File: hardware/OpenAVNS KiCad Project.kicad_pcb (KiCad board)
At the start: 4 copper layers, 69.9 x 100.9 mm, 216 parts, among them J1 Conn_ARM_JTAG_SWD_10, J2 AudioPlug3, J3 USB_C_Receptacle, J4 Conn_01x02_Pin, J5 Conn_01x03_Pin, J6 Conn_01x01_Pin, Q1 BCV62, Q2 BC847, Q3 BC857, Q4 BCV61, Q5 BCV62, Q6 BC847, Q7 BC857, Q8 BCV61, SW1 SW_SPDT, T1 Wurth 750315839 - 1:10, 40uH, U1 TS5A3159AYZPR, U10 TLV9062, U11 LIS2DH12, U12 OPA455, U13 74AUC1G74, U14 TPS61200DRC, U15 LT1615ES5_TRPBF, U16 LT8304IS8E_PBF, U17 MCP73831-2-OT, U2 TLV9004xRUCR, U3 MCP4725xxx-xCH, U4 TS5A3159AYZPR, U5 nRF52840, U6 TS5A3159AYZPR, U7 MCP4725xxx-xCH, U8 TS5A3159AYZPR, U9 OPA455, Y1 32MHz - X322532MOB4SI

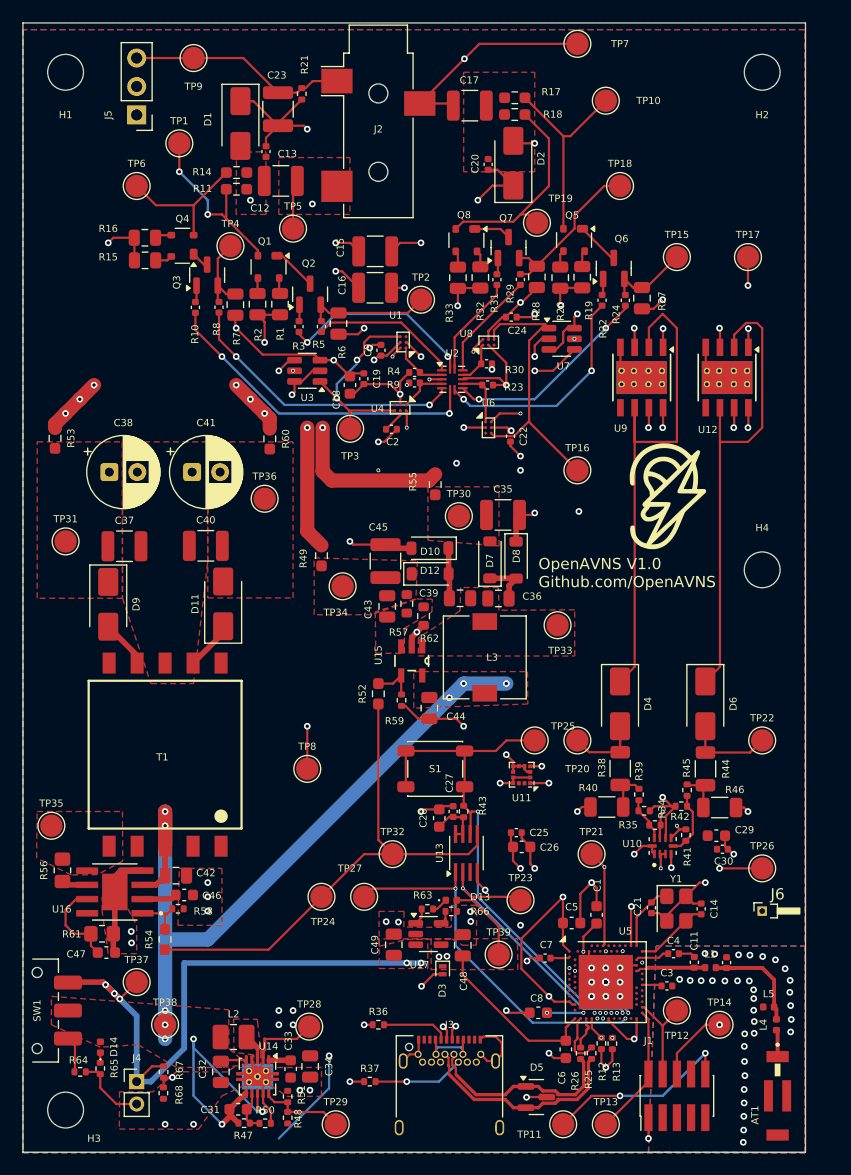
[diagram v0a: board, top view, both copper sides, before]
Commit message: Fixed hole clearance DRC errors
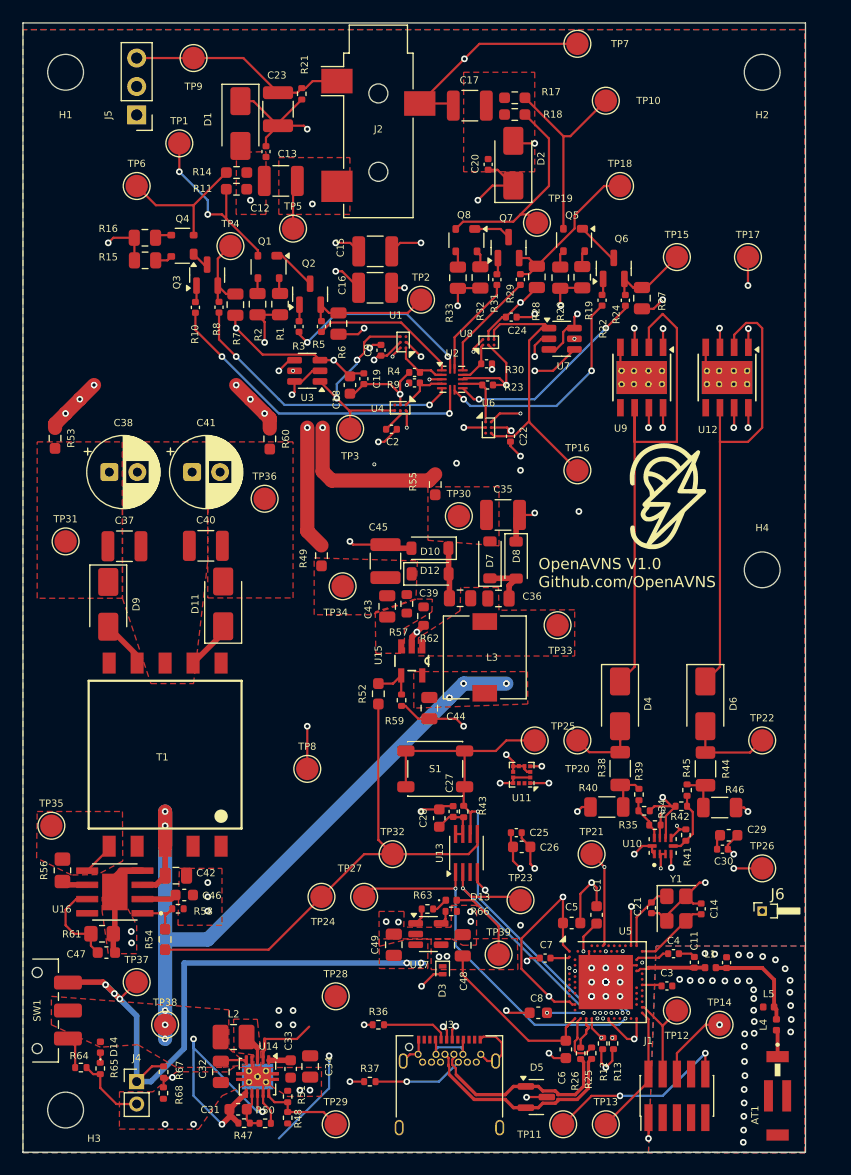
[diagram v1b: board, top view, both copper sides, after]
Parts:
- moved TP28 3.60 mm to (86.4, 132.1)
- moved C29 1.10 mm to (121.5, 117.7)
- moved R64 0.39 mm to (63.6, 138.4)
- moved R12 0.12 mm to (110.2, 136.3)
- moved R13 0.10 mm to (111.2, 136.3)
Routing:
- net Net-(U16-SW): track 0.00 -> 2.99 mm
- net +3.3V: track 155.3 -> 156.8 mm
- net /C2A_ON: track 78.8 -> 80.3 mm
- net /I2C_SDA: track 94.4 -> 95.4 mm

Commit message: Edited based on Maros advice, thanks
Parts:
- moved TP1 5.39 mm to (68.6, 59.7)
- moved TP6 5.39 mm to (72.4, 55.9)
- moved C32 1.93 mm to (74.2, 138.7)
- moved C31 1.53 mm to (76.3, 141.5), turned to -90 degrees
- moved L2 1.02 mm to (76.7, 134.9)
- moved R54 0.67 mm to (71.8, 127.0)
- moved R50 0.56 mm to (80.6, 143.4)
- moved R58 0.42 mm to (72.2, 124.7)
- moved C46 0.32 mm to (72.8, 123.3)
- moved L5 0.31 mm to (125.3, 133.1)
- moved R47 0.14 mm to (78.3, 143.4)
- moved L4 0.13 mm to (125.8, 134.7)
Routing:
- net GND: track 173.2 -> 161.4 mm
- net Net-(U7-VOUT): track 25.8 -> 32.8 mm
- net +3.3V: track 156.8 -> 150.7 mm, vias 26 -> 23
- net Net-(D6-K): track 42.4 -> 46.0 mm
- net Net-(U14-UVLO): track 3.85 -> 6.61 mm
- net Net-(D4-K): track 47.3 -> 44.5 mm
- net /C2_Anodic: track 18.2 -> 20.4 mm
- net /C1_Cathodic: track 12.6 -> 14.0 mm, vias 0 -> 2
- net /C1_Anodic: track 16.3 -> 15.2 mm, vias 2 -> 0
- net Net-(U14-L): track 2.46 -> 3.55 mm
- net /V_ON: track 95.9 -> 96.9 mm
- net /50V_ON: track 4.92 -> 4.07 mm
- net Net-(J1-SWCLK/TCK): track 8.71 -> 9.42 mm
- net /HV_ON: track 46.7 -> 46.0 mm
- net Net-(U3-VOUT): track 18.9 -> 19.5 mm
- removed copper zone on F.Cu, net Net-(U14-L)

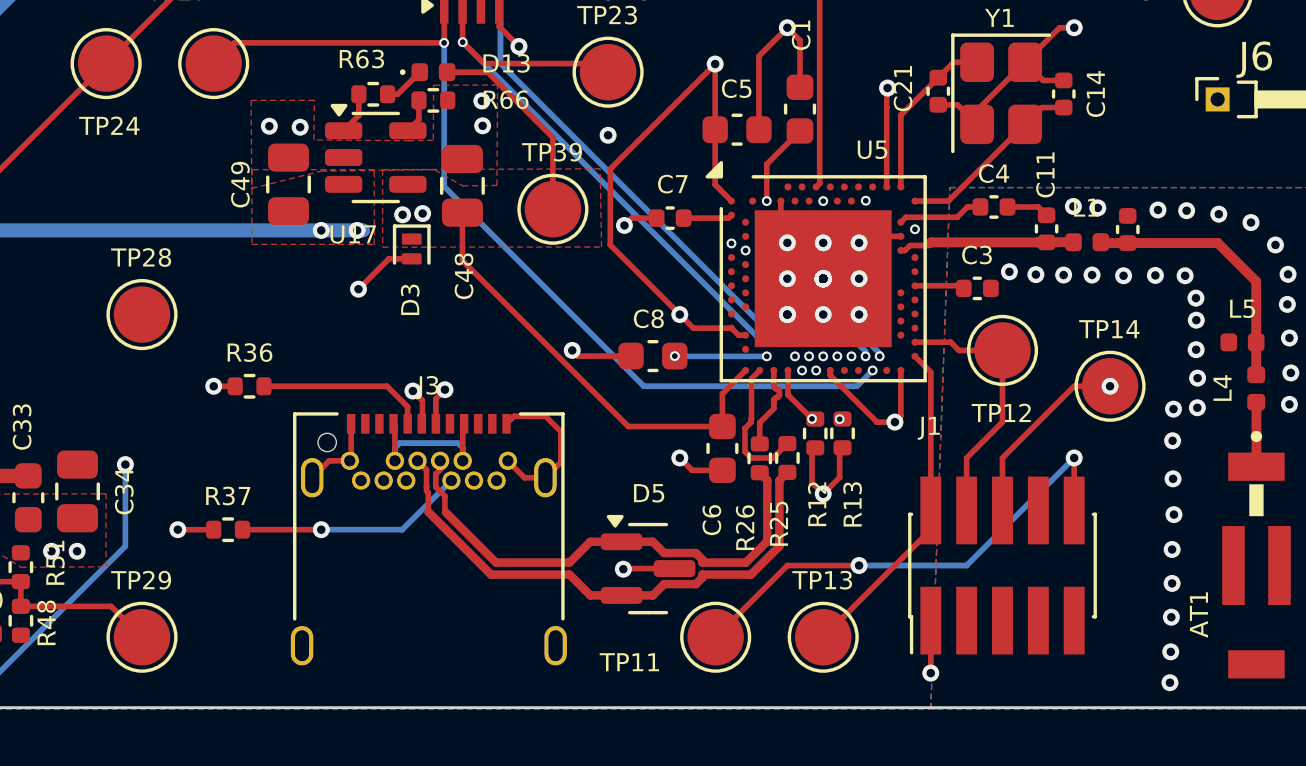
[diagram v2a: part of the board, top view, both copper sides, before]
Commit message: Updated USB connector and routing
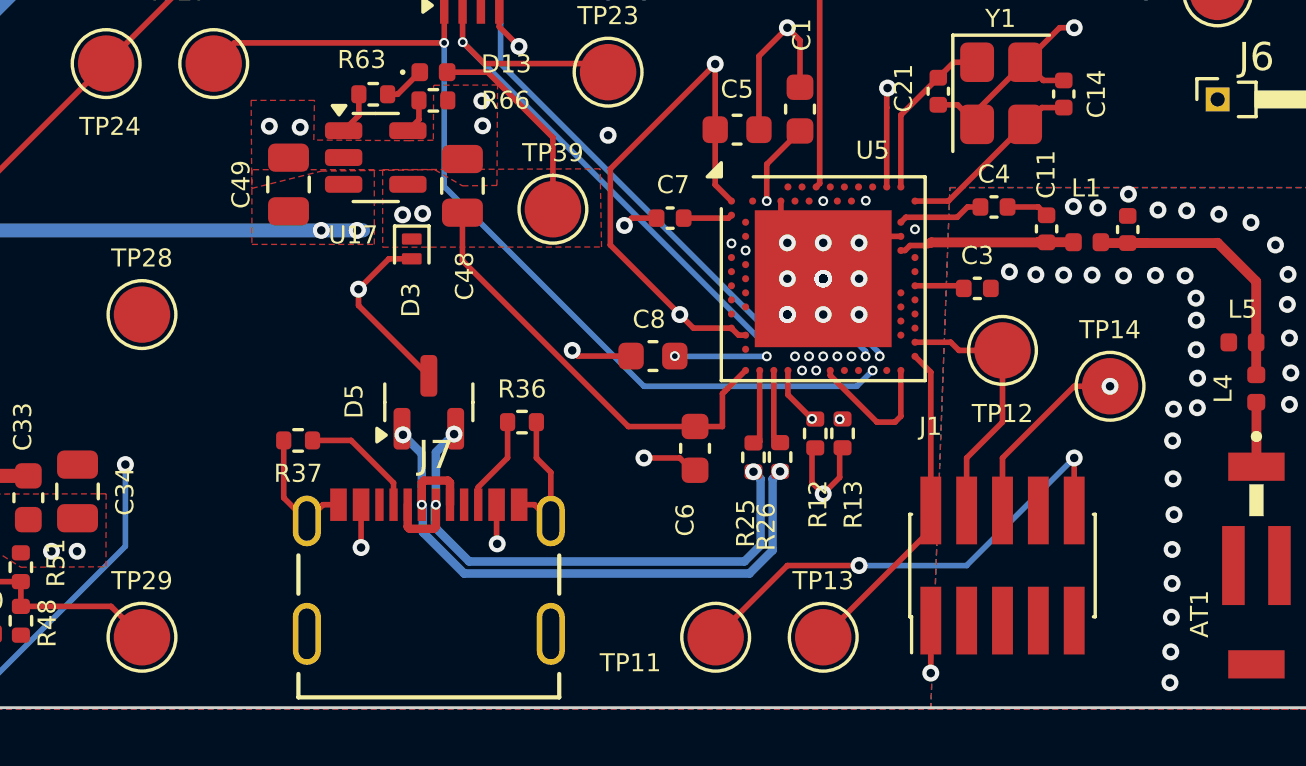
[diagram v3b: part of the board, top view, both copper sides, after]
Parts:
- removed J3: USB_C_Receptacle, Connector_USB:USB_C_Receptacle_Amphenol_12401548E4-2A
- added J7: 2171790001, Footprints:MOLEX_2171790001, F.Cu at (96.5, 142.2)
- R15: value R_US -> 1k
- R16: value R_US -> 150 Ohm
- R29: value R_US -> 100 Ohm
- moved D5 9.75 mm to (96.5, 135.2), turned to 90 degrees
- moved R36 9.73 mm to (99.8, 135.9)
- moved R37 4.02 mm to (91.9, 136.5), turned to 180 degrees
- moved R25 1.20 mm to (108.0, 137.1)
- moved C6 0.97 mm to (106.0, 136.8)
- moved R26 0.72 mm to (109.0, 137.1)
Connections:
- R36 pad 1: GND -> Net-(J7-CC2)
- R36 pad 2: Net-(J3-CC1) -> GND
- R37 pad 1: GND -> Net-(J7-CC1)
- R37 pad 2: Net-(J3-CC2) -> GND
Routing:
- net Net-(J3-CC2): track 8.12 -> 0.00 mm, vias 1 -> 0
- net Net-(J3-CC1): track 5.99 -> 0.00 mm
- net /V_USB: track 31.8 -> 25.8 mm, vias 2 -> 4
- net Net-(J7-CC1): track 0.00 -> 4.27 mm
- net Net-(J7-CC2): track 0.00 -> 3.36 mm
- net /MCU_D-: track 4.90 -> 2.64 mm
- net /USB_D-: track 23.4 -> 21.2 mm, vias 1 -> 3
- net GND: track 161.4 -> 163.3 mm, vias 111 -> 109
- net /USB_D+: track 22.0 -> 22.6 mm, vias 1 -> 3
- net +3.3V: vias 23 -> 22

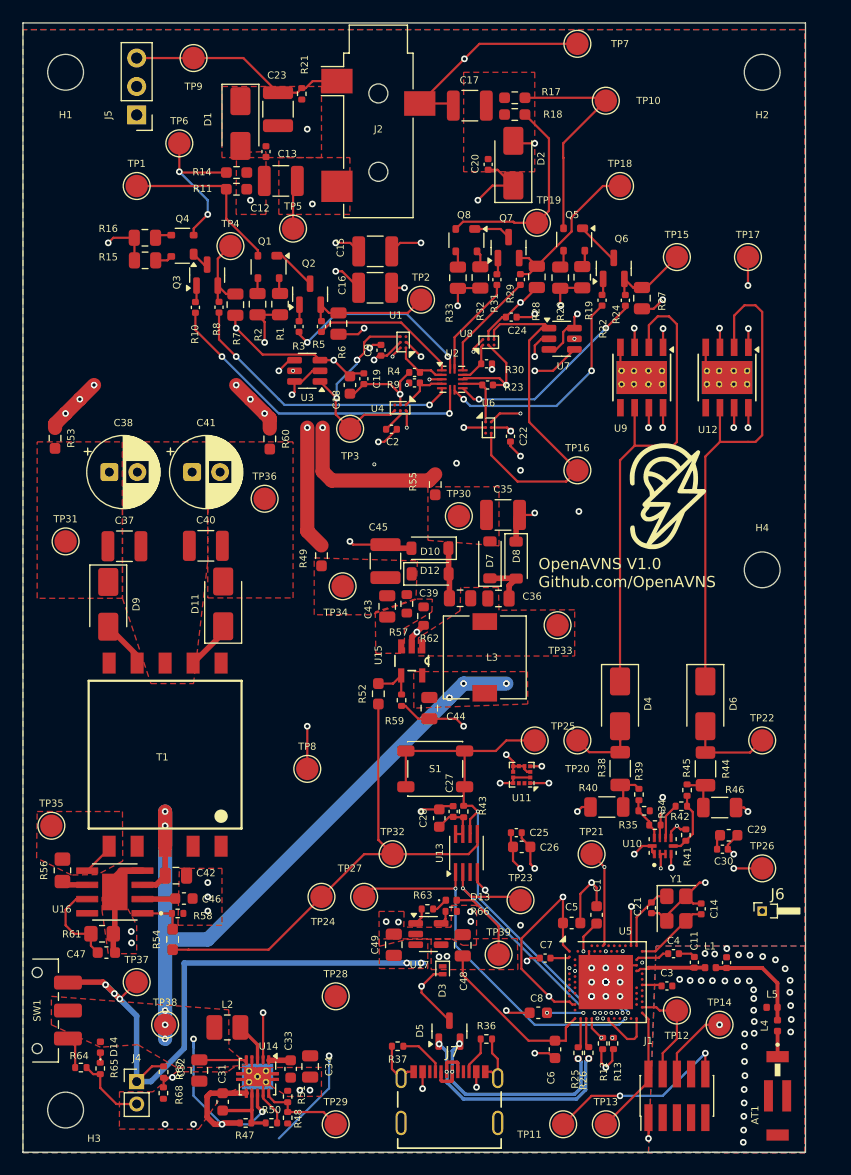
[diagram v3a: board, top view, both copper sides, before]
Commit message: Replaced zero ohm resistors with headers
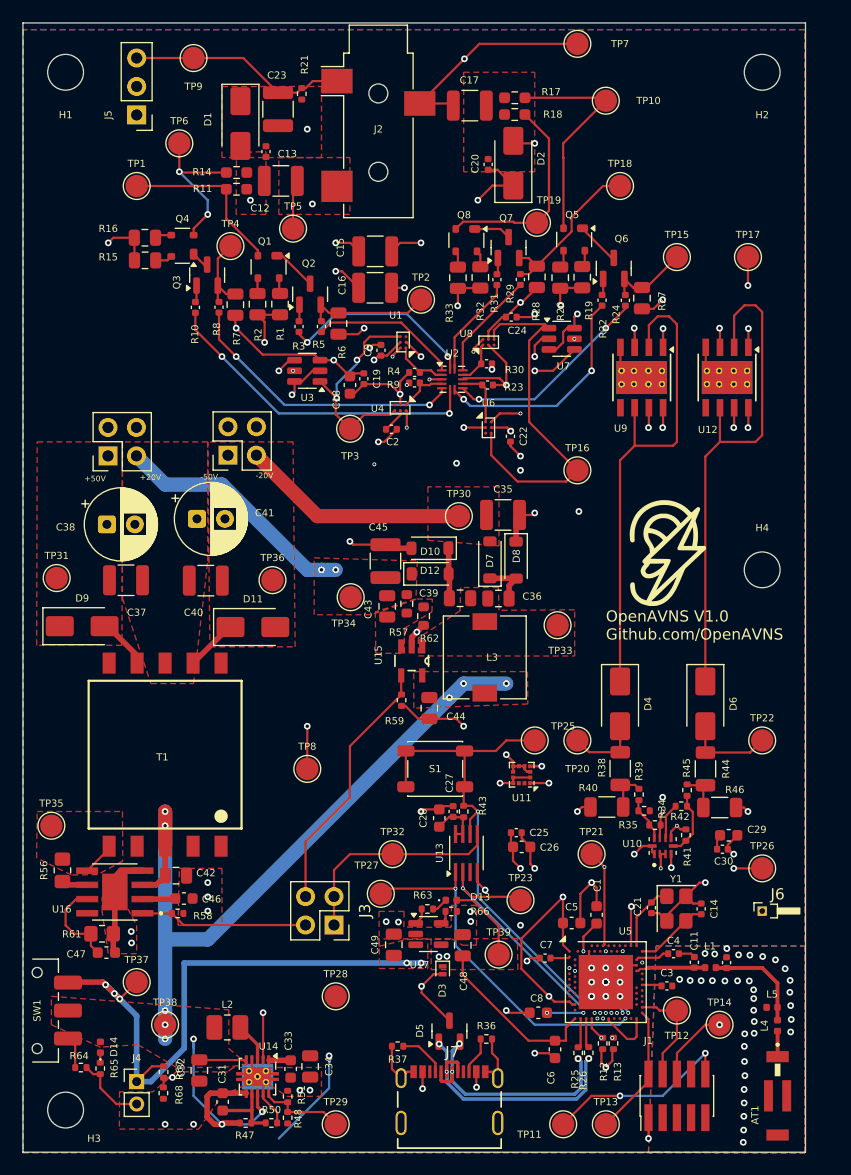
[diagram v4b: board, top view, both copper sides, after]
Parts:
- removed R49, R52, R53, R54, R55, R60: 0 Ohm, Resistor_SMD:R_0603_1608Metric_Pad0.98x0.95mm_HandSolder
- removed TP24: TestPoint, TestPoint:TestPoint_Pad_D2.0mm
- added J3: Conn_02x02_Top_Bottom, Connector_PinSocket_2.54mm:PinSocket_2x02_P2.54mm_Vertical, F.Cu at (86.2, 125.7)
- added J8: Conn_02x02_Top_Bottom, Connector_PinSocket_2.54mm:PinSocket_2x02_P2.54mm_Vertical, F.Cu at (66.0, 83.8)
- added J9: Conn_02x02_Top_Bottom, Connector_PinSocket_2.54mm:PinSocket_2x02_P2.54mm_Vertical, F.Cu at (76.7, 83.7)
- moved TP36 7.30 mm to (80.7, 94.9)
- moved G*** 5.08 mm to (115.6, 92.7)
- moved C38 4.68 mm to (65.9, 89.9)
- moved C41 4.20 mm to (74.0, 89.4)
- moved TP31 3.37 mm to (61.4, 94.7)
- moved D11 3.37 mm to (79.0, 99.1), turned to 0 degrees
- moved C40 3.11 mm to (74.8, 94.9)
- moved C37 3.04 mm to (67.6, 94.9)
- moved D9 3.04 mm to (63.7, 99.0), turned to 0 degrees
- moved TP27 1.51 mm to (90.4, 122.9)
- moved TP34 1.21 mm to (87.7, 96.4)
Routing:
- net /HV_ON: track 46.0 -> 19.6 mm
- net /+20V: track 0.00 -> 22.0 mm, vias 0 -> 2
- net /-20V: track 0.00 -> 20.3 mm
- net /-HV: track 34.7 -> 15.1 mm, vias 7 -> 3
- net /20V_ON: track 4.06 -> 23.3 mm
- net /+HV: track 30.6 -> 14.3 mm, vias 9 -> 5
- net /50V_ON: track 4.07 -> 15.1 mm
- net /HV_CLK: track 33.4 -> 31.8 mm
- net GND: track 163.3 -> 162.5 mm
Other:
- board text added: "+20V"
- board text added: "+50V"
- board text added: "-20V"
- board text added: "-50V"

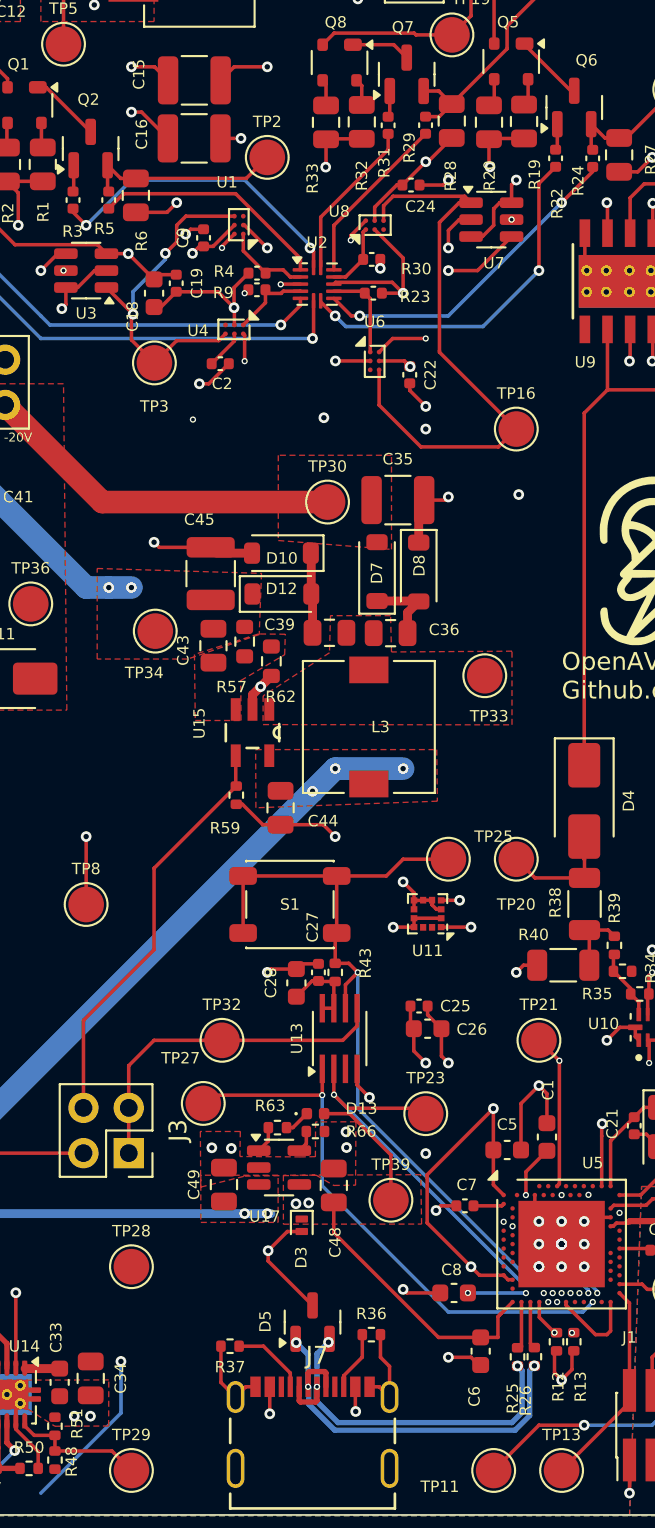
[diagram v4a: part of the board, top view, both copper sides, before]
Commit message: Updated footprint of switches based on component availability
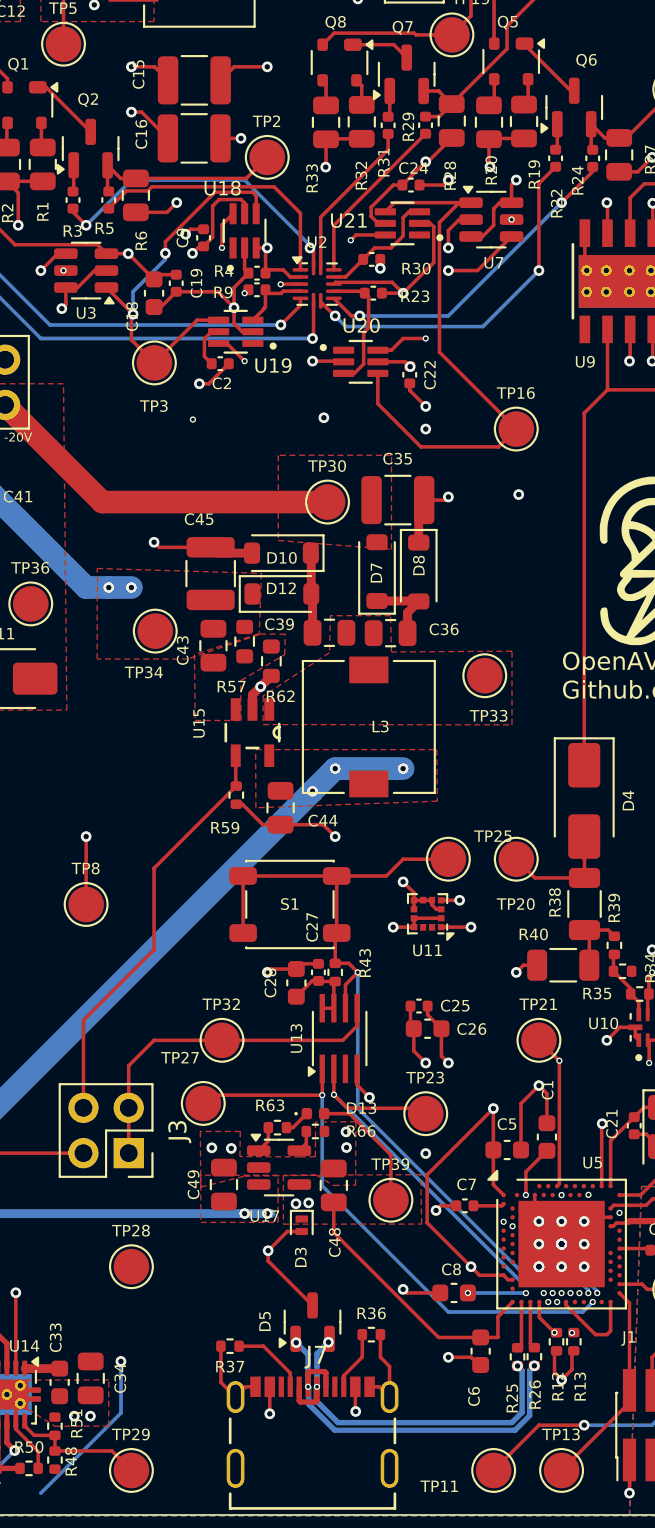
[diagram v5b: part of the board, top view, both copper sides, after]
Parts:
- removed U1, U4, U6, U8: TS5A3159AYZPR, Package_BGA:Texas_DSBGA-6_0.9x1.4mm_Layout2x3_P0.5mm
- added U18: TS5A3159DCKR, Footprints:SOT65P210X110-6N, F.Cu at (92.7, 74.0)
- added U19: TS5A3159DCKR, Footprints:SOT65P210X110-6N, F.Cu at (92.2, 79.6)
- added U20: TS5A3159DCKR, Footprints:SOT65P210X110-6N, F.Cu at (99.2, 81.3)
- added U21: TS5A3159DCKR, Footprints:SOT65P210X110-6N, F.Cu at (101.6, 73.6)
- C15, C16: value 22uF, 100V -> 22uF
- C35, C45: value 22uF, 100V -> 22uF, 25V
- C42: value 22uF, 50V -> 22uF, 6.3V
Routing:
- net +3.3V: track 150.7 -> 154.9 mm
- net Net-(U2D-+): track 3.79 -> 6.92 mm
- net Net-(U3-VOUT): track 19.5 -> 22.2 mm
- net Net-(U2C-+): track 5.21 -> 7.30 mm
- net Net-(U2A--): track 13.2 -> 15.0 mm
- net Net-(U7-VOUT): track 32.8 -> 31.5 mm
- net GND: track 162.5 -> 163.7 mm, vias 109 -> 108
- net /C1A_ON: track 70.6 -> 71.8 mm
- net Net-(U2A-+): track 4.91 -> 4.27 mm, vias 0 -> 1
- net /C2C_ON: track 68.3 -> 68.9 mm
